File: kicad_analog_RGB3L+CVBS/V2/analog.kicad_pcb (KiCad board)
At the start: 2 copper layers, 50 x 23.2 mm, 22 parts, among them P1 Conn_02x05_Odd_Even, P2 Conn_01x04, P3 Conn_01x05, P4 Conn_01x02, P6 Conn_01x01, P7 Conn_01x01, U1 MAX9144, U2 MAX9144, U3 4066, U4 MCP1754S-3302xCB, U5 MAX5259EEE+

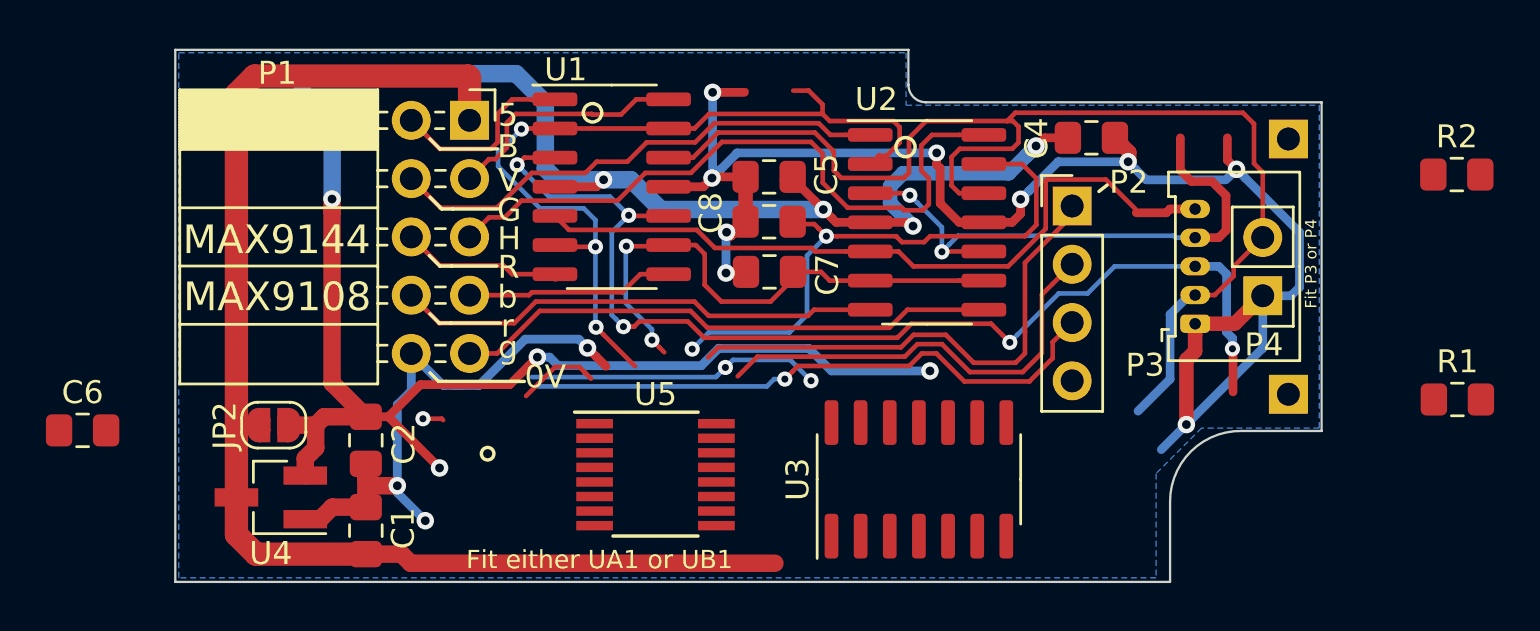
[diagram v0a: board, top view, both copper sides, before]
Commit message: Terminator and decoupling caps added plus pcb layout
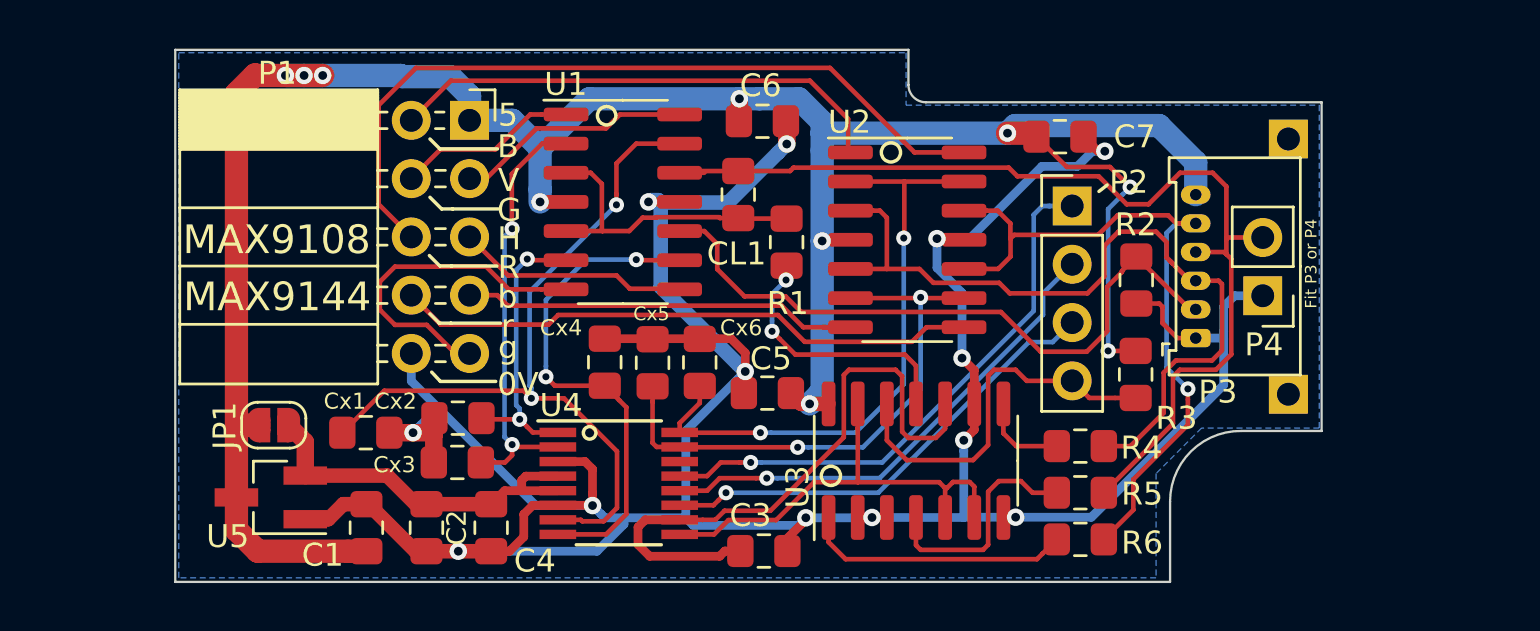
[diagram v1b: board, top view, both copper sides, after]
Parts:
- removed JP4: SolderJumper_3_Bridged12, Jumper:SolderJumper-3_P1.3mm_Bridged12_RoundedPad1.0x1.5mm_NumberLabels
- removed the U1 at (46.6, 37.3)
- added C6: 100n, Capacitor_SMD:C_0805_2012Metric_Pad1.15x1.40mm_HandSolder, F.Cu at (53.1, 34.4)
- added Cx1: 100n, Capacitor_SMD:C_0805_2012Metric_Pad1.15x1.40mm_HandSolder, F.Cu at (35.8, 48.0)
- added Cx2: 100n, Capacitor_SMD:C_0805_2012Metric_Pad1.15x1.40mm_HandSolder, F.Cu at (39.8, 47.4)
- added Cx3: 100n, Capacitor_SMD:C_0805_2012Metric_Pad1.15x1.40mm_HandSolder, F.Cu at (39.8, 49.3)
- added Cx4: 100n, Capacitor_SMD:C_0805_2012Metric_Pad1.15x1.40mm_HandSolder, F.Cu at (46.2, 44.9)
- added Cx5: 100n, Capacitor_SMD:C_0805_2012Metric_Pad1.15x1.40mm_HandSolder, F.Cu at (48.3, 44.9)
- added Cx6: 100n, Capacitor_SMD:C_0805_2012Metric_Pad1.15x1.40mm_HandSolder, F.Cu at (50.4, 44.9)
- added R1: 75R, Resistor_SMD:R_0805_2012Metric_Pad1.15x1.40mm_HandSolder, F.Cu at (54.2, 39.7)
- added R4: 75R, Resistor_SMD:R_0805_2012Metric_Pad1.15x1.40mm_HandSolder, F.Cu at (67.0, 48.6)
- added R5: 75R, Resistor_SMD:R_0805_2012Metric_Pad1.15x1.40mm_HandSolder, F.Cu at (67.0, 50.6)
- added R6: 75R, Resistor_SMD:R_0805_2012Metric_Pad1.15x1.40mm_HandSolder, F.Cu at (67.0, 52.6)
- added U2: MAX9144, Package_SO:SOIC-14_3.9x8.7mm_P1.27mm, F.Cu at (59.4, 39.6)
- P3: value Conn_01x05 -> Conn_01x06; footprint Connector_Molex:Molex_PicoBlade_53048-0510_1x05_P1.25mm_Horizontal -> Connector_Molex:Molex_PicoBlade_53048-0610_1x06_P1.25mm_Horizontal
- moved C4 18.3 mm to (41.3, 52.1), turned to 270 degrees
- moved R2 14.7 mm to (69.4, 41.3), turned to 270 degrees
- moved R3 14.1 mm to (69.4, 45.5), turned to 270 degrees
- moved U1 13.3 mm to (47.0, 37.9)
- moved C3 12.2 mm to (53.2, 53.1), turned to 0 degrees
- moved C5 9.42 mm to (53.3, 46.3)
- moved C2 4.64 mm to (38.5, 52.1)
- moved CL1 1.79 mm to (52.1, 37.6), turned to 270 degrees
- moved U4 1.64 mm to (46.9, 50.2)
- moved C7 1.37 mm to (66.1, 35.1)
- moved U3 0.82 mm to (59.8, 49.2)
- moved P3 0.63 mm to (72.0, 43.9)
- moved C1 0.13 mm to (35.9, 52.1)
- renumbered C7 to C3, C6 to C4, C4 to C7, C8 to CL1, JP2 to JP1, R1 to R3, U2 to U1, U5 to U4, U4 to U5
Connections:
- C5 pad 1: /OPAMP_PWR -> /VCC
- C7 pad 1: /OPAMP_PWR -> /VCC
- P3 pad 1: Net-(P3-Pad1) -> /GND
- P4 pad 1: Net-(P3-Pad1) -> /GND
- P4 pad 2: /ASYNC -> /AGREEN
- U1 pad 10: /CGREEN -> /ASYNC
- U1 pad 12: /ASYNC -> /AGREEN
- U1 pad 13: /SYNCLVL -> /REFGYSYNC
- U1 pad 14: /SYNC -> /VSYNC
- U1 pad 2: /GYMED -> /REFGYHI
- U1 pad 4: /OPAMP_PWR -> /VCC
- U1 pad 5: /ARED -> /CGREEN
- U1 pad 6: /RBUVLO -> /REFGYLO
- U1 pad 7: /BRED -> /BGREEN
- U1 pad 8: /BGREEN -> /SYNC
- U1 pad 9: /GYLO -> /REFSYNC
- U3 pad 1: /ABLUE -> Net-(R6-Pad2)
- U3 pad 11: /CGREEN -> Net-(R1-Pad2)
- U3 pad 4: /AGREEN -> Net-(R5-Pad2)
- U3 pad 8: /ARED -> Net-(R4-Pad2)
- U4 pad 1: /RBUVHI -> /REFGYLO
- U4 pad 15: /GYMED -> /REFRBUVLO
- U4 pad 16: /GYHI -> /REFRBUVHI
- U4 pad 2: /RBUVLO -> /REFGYHI
- U4 pad 7: /GYLO -> /REFGYSYNC
- U4 pad 8: /SYNCLVL -> /REFSYNC
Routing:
- net /VCC: track 58.1 -> 111.3 mm, vias 1 -> 10
- net /OPAMP_PWR: track 48.4 -> 0.00 mm, vias 4 -> 0
- net /GND: track 98.8 -> 146.3 mm, vias 12 -> 13
- net /REF100: track 41.1 -> 0.00 mm, vias 3 -> 0
- net /REFGYSYNC: track 0.00 -> 34.1 mm, vias 0 -> 2
- net /VANALOG: track 49.5 -> 16.4 mm, vias 4 -> 0
- net /CLAMPLVL: track 0.00 -> 27.2 mm
- net /RED: track 6.99 -> 33.9 mm
- net /REFRBUVHI: track 0.00 -> 26.8 mm, vias 0 -> 2
- net /REFRBUVLO: track 0.00 -> 24.3 mm, vias 0 -> 2
- net /REF50: track 23.7 -> 0.00 mm, vias 2 -> 0
- net /ASYNC: track 52.6 -> 29.2 mm
- net /AGREEN: track 25.3 -> 46.3 mm, vias 2 -> 0
- net /SYNC: track 29.4 -> 10.1 mm
- net /REFGYHI: track 0.00 -> 19.0 mm, vias 0 -> 2
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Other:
- board text added: "+5V"
- board text added: "MAX9108 / MAX9144 Issue 2 ©2019 IanB"
- board text added: "Three level analog RGB/YUV & composite"
- board text removed: "Fit either UA1 or UB1"
- board text removed: "MAX9144 / MAX9108 Issue 1 ©2019 IanB"
- board text removed: "Three level analog RGB & composite"

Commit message: Add gerbers
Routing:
- net /GND: track 146.3 -> 144.3 mm
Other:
- board text added: "0"
- board text removed: "0V"
